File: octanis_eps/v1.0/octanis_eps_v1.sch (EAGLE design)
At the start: 156 parts, among them Q1 CSD16327Q3_DQG_8, Q2 CSD16327Q3_DQG_8, Q3 CSD16327Q3_DQG_8, Q4 BSS123, Q5 CSD16327Q3_DQG_8, Q6 CSD16327Q3_DQG_8, Q7 BSC0901NS, U1 MSP430FR5969, U10 INA213, U11 MIC5019, U12 TPS61088, U2 OPA2333DGK, U3 TPS2022D, U4 TPS630250YFFT, U5 BQ24650_RVA_16, U6 TPS630250YFFT, U7 TPS61232, U8 TPS630250YFFT, U9 INA213, X1 32.768kHz

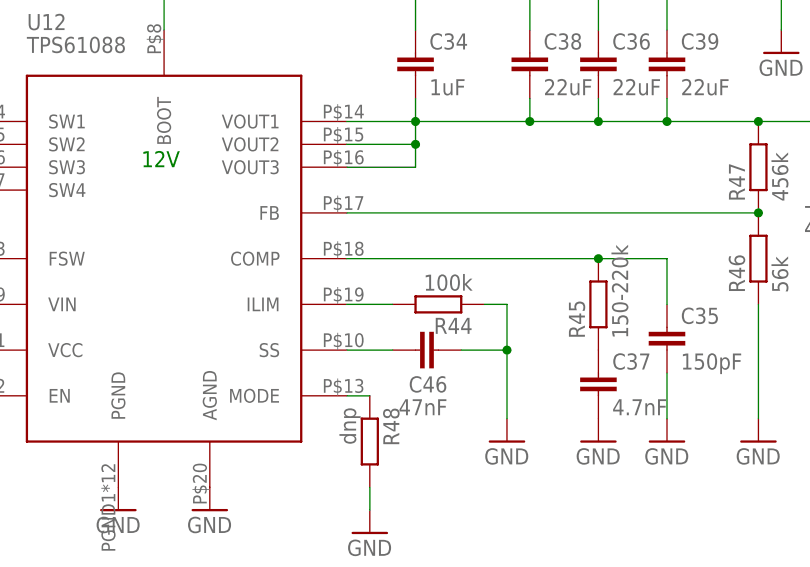
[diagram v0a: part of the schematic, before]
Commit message: EPS v2.0 finished routing
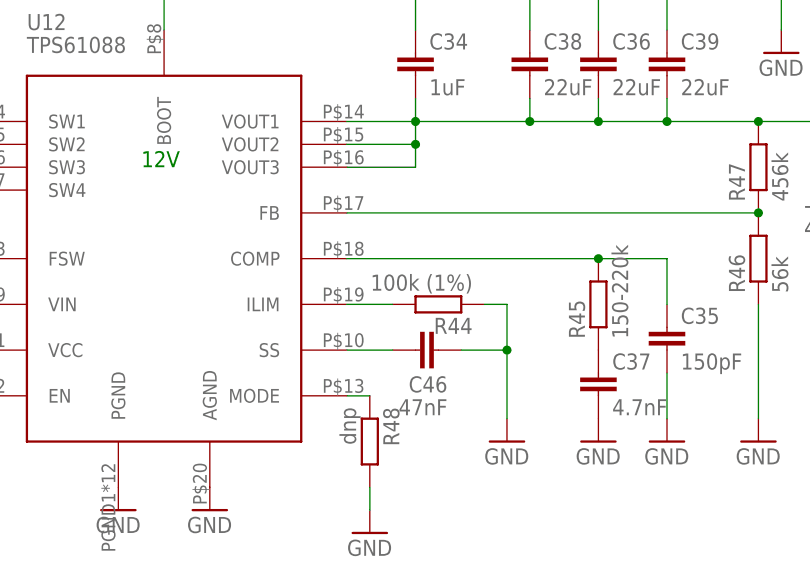
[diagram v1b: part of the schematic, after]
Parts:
- R44: value 100k -> 100k (1%)
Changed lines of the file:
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@@
 <part name="C33" library="rcl" deviceset="C-EU" device="C0603" value="2.2uF"/>
 <part name="C46" library="rcl" deviceset="C-EU" device="C0603" value="47nF"/>
-<part name="R44" library="resistor" deviceset="R-EU_" device="R0603" value="100k"/>
+<part name="R44" library="resistor" deviceset="R-EU_" device="R0603" value="100k (1%)"/>
 <part name="R45" library="resistor" deviceset="R-EU_" device="R0603" value="150-220k"/>
 <part name="C35" library="rcl" deviceset="C-EU" device="C0603" value="150pF"/>
